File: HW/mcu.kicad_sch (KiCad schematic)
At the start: 12 parts, among them J2 JTAG, SW2 SW_DPST, SW3 SW_DPST, U1 ESP32-S2-MINI-2

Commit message: revision 0
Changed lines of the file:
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@@
     (stroke (width 0) (type default) (color 0 0 0 0))
   )
-  (wire (pts (xy 109.22 62.23) (xy 124.46 62.23))
+  (wire (pts (xy 109.22 62.23) (xy 123.19 62.23))
     (stroke (width 0) (type default) (color 0 0 0 0))
   )
@@
     (effects (font (size 5 5)) (justify left bottom))
   )
-  (label "activity_led" (at 124.46 62.23 180)
+  (label "activity_led" (at 123.19 62.23 180)
     (effects (font (size 1.27 1.27)) (justify right bottom))
   )

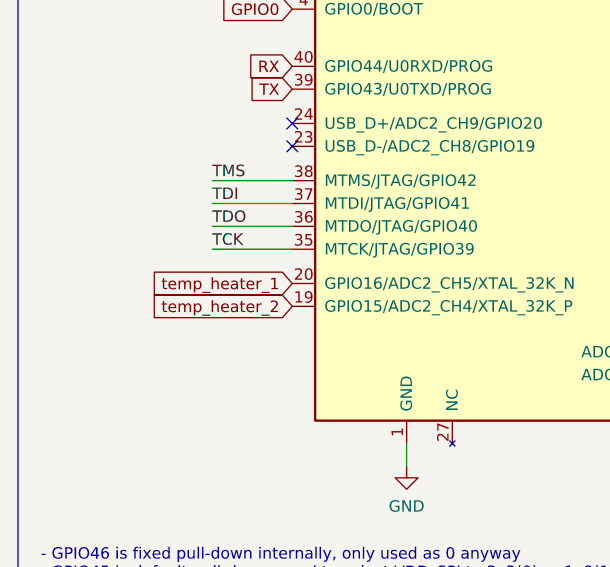
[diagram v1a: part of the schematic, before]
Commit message: Fixed silkscreen, removed one thermistor, fixed component placement
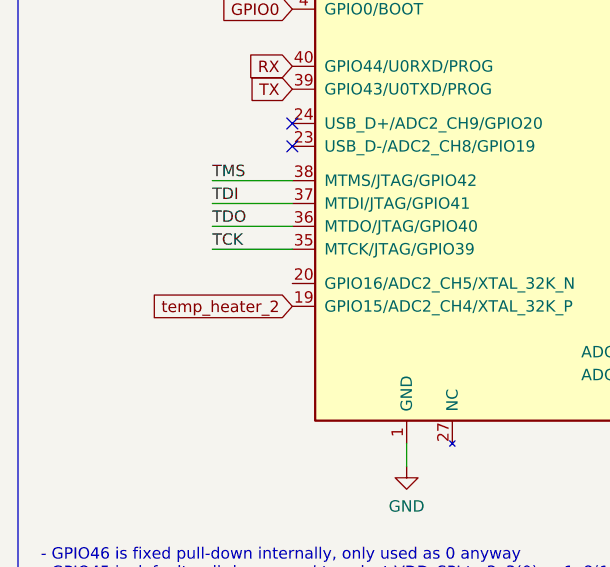
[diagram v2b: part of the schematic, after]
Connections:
- net temp_heater_1: no longer names the net of U1.20 (GPIO16/ADC2_CH5/XTAL_32K_N)
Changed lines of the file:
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@@
-    )
-  )
-  (global_label "temp_heater_1" (shape input) (at 48.26 87.63 180) (fields_autoplaced)
-    (effects (font (size 1.27 1.27)) (justify right))
-    (property "Intersheet References" "${INTERSHEET_REFS}" (id 0) (at 32.0583 87.5506 0)
-      (effects (font (size 1.27 1.27)) (justify right) hide)
     )
   )

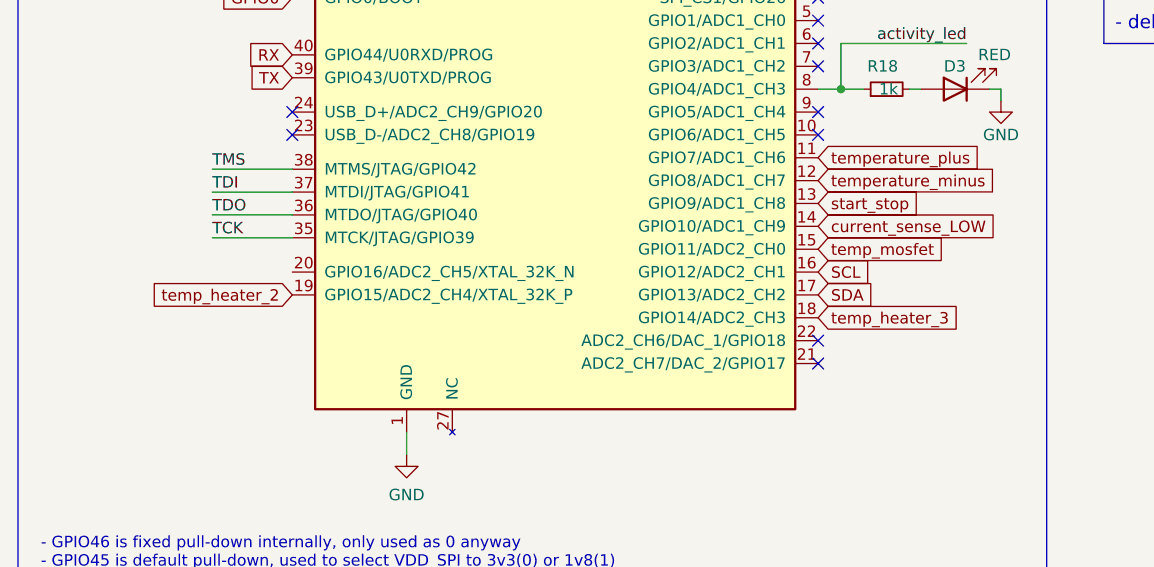
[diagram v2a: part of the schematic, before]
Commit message: Fixed component placement, enlarged some pcb slots, removed two thermistors
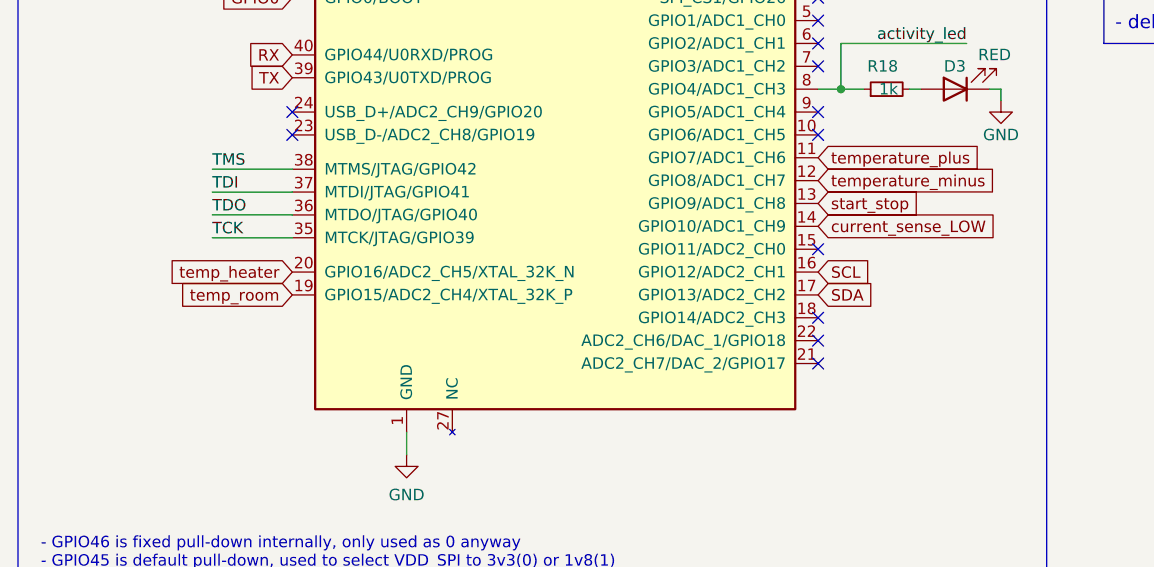
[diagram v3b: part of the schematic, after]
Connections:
- net temp_heater: now reaches U1.20 (GPIO16/ADC2_CH5/XTAL_32K_N)
- net temp_heater_2 renamed temp_room
- net temp_heater_3: no longer names the net of U1.18 (GPIO14/ADC2_CH3)
- net temp_mosfet: no longer names the net of U1.15 (GPIO11/ADC2_CH0)
- no-connect marks 18 -> 20
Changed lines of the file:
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@@
   (no_connect (at 48.26 69.85))
   (no_connect (at 106.68 64.77))
+  (no_connect (at 106.68 85.09))
   (no_connect (at 106.68 52.07))
   (no_connect (at 106.68 41.91))
@@
   (no_connect (at 48.26 72.39))
   (no_connect (at 106.68 95.25))
+  (no_connect (at 106.68 92.71))
   (no_connect (at 106.68 49.53))
   (no_connect (at 106.68 46.99))
@@
     (effects (font (size 1.27 1.27)) (justify left bottom))
   )
-  (global_label "temp_heater_3" (shape input) (at 106.68 92.71 0) (fields_autoplaced)
-    (effects (font (size 1.27 1.27)) (justify left))
-    (property "Intersheet References" "${INTERSHEET_REFS}" (id 0) (at 122.8817 92.7894 0)
-      (effects (font (size 1.27 1.27)) (justify left) hide)
-    )
-  )
   (global_label "GPIO0" (shape input) (at 190.5 40.64 180) (fields_autoplaced)
     (effects (font (size 1.27 1.27)) (justify right))
@@
     )
   )
-  (global_label "temp_mosfet" (shape input) (at 106.68 85.09 0) (fields_autoplaced)
-    (effects (font (size 1.27 1.27)) (justify left))
-    (property "Intersheet References" "${INTERSHEET_REFS}" (id 0) (at 121.1279 85.1694 0)
-      (effects (font (size 1.27 1.27)) (justify left) hide)
+  (global_label "temp_heater" (shape input) (at 48.26 87.63 180) (fields_autoplaced)
+    (effects (font (size 1.27 1.27)) (justify right))
+    (property "Intersheet References" "${INTERSHEET_REFS}" (id 0) (at 34.2355 87.5506 0)
+      (effects (font (size 1.27 1.27)) (justify right) hide)
+    )
+  )
+  (global_label "temp_room" (shape input) (at 48.26 90.17 180) (fields_autoplaced)
+    (effects (font (size 1.27 1.27)) (justify right))
+    (property "Intersheet References" "${INTERSHEET_REFS}" (id 0) (at 35.445 90.0906 0)
+      (effects (font (size 1.27 1.27)) (justify right) hide)
     )
   )
@@
       (effects (font (size 1.27 1.27)) (justify right) hide)
     )
-  )
-  (global_label "temp_heater_2" (shape input) (at 48.26 90.17 180) (fields_autoplaced)
-    (effects (font (size 1.27 1.27)) (justify right))
-    (property "Intersheet References" "${INTERSHEET_REFS}" (id 0) (at 32.0583 90.0906 0)
-      (effects (font (size 1.27 1.27)) (justify right) hide)
-    )
